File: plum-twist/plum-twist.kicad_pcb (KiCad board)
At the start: 2 copper layers, 17 x 17.9 mm, 9 parts, among them J2 Conn_01x04_Male, J6 Conn_01x01_Male

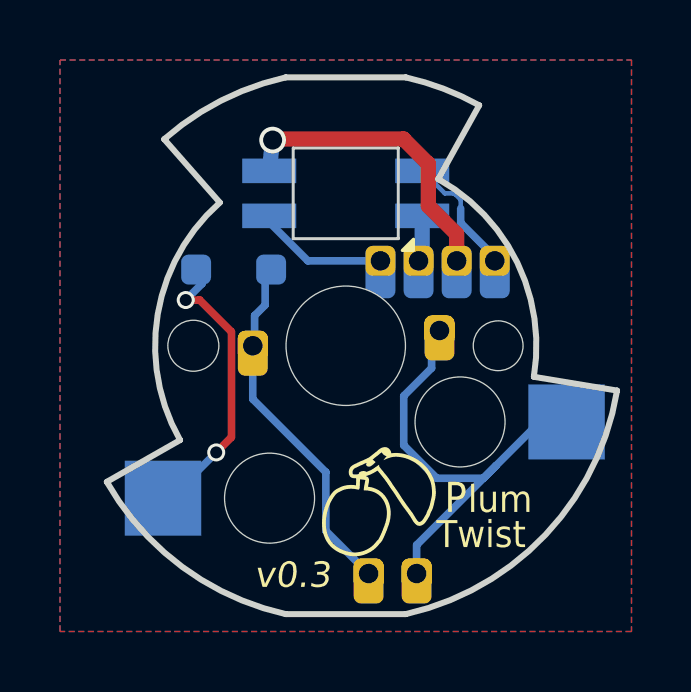
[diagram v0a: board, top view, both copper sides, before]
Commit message: Bring Plum Twist in repo up to date with store version
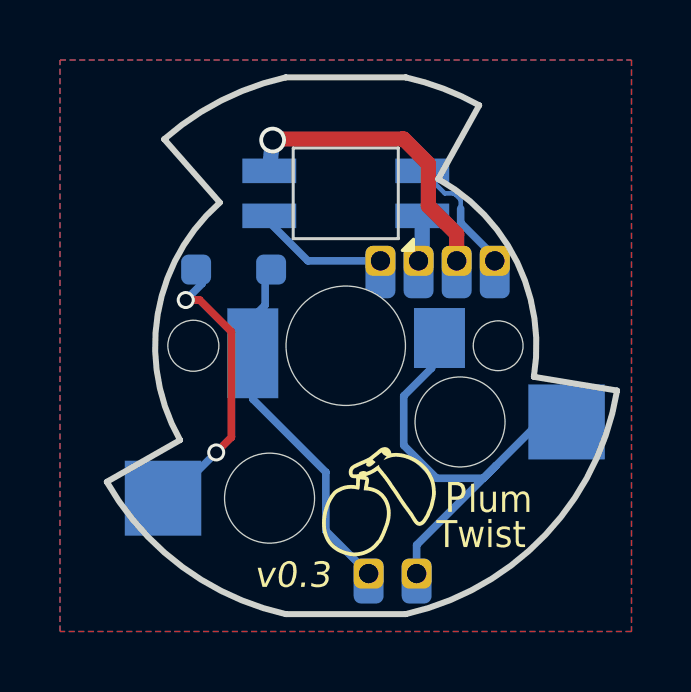
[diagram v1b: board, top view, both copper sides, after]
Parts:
- removed the J6 at (78.6, 168.1)
- removed the J6 at (77.8, 176.2)
- removed the J6 at (72.3, 168.7)
- removed the J6 at (76.2, 176.2)
- added J6: Conn_01x01_Male, amoeba-modules:Header_1x01_P1.27mm, B.Cu at (72.3, 168.7)
- added J6: Conn_01x01_Male, amoeba-modules:Header_1x01_P1.27mm, B.Cu at (76.2, 176.2)
- added J6: Conn_01x01_Male, amoeba-modules:Header_1x01_P1.27mm, B.Cu at (77.8, 176.2)
- added J6: Conn_01x01_Male, amoeba-modules:Header_1x01_P1.27mm, B.Cu at (78.6, 168.1)
